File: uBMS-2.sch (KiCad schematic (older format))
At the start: 65 parts

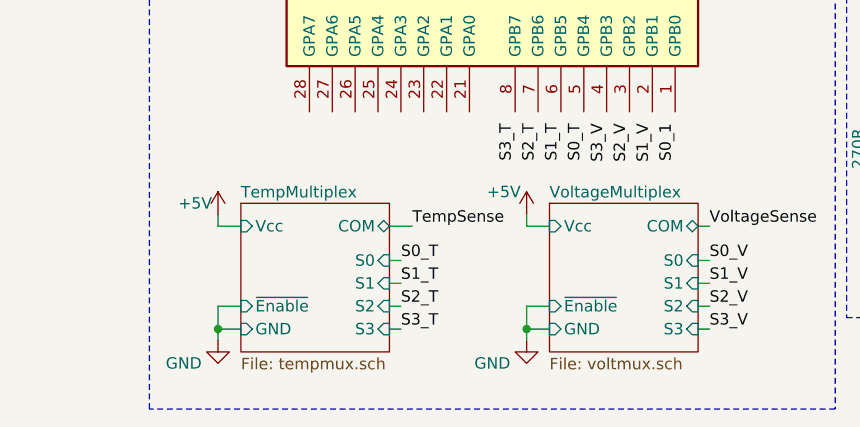
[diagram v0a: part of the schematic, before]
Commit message: Work on Voltage Sheet
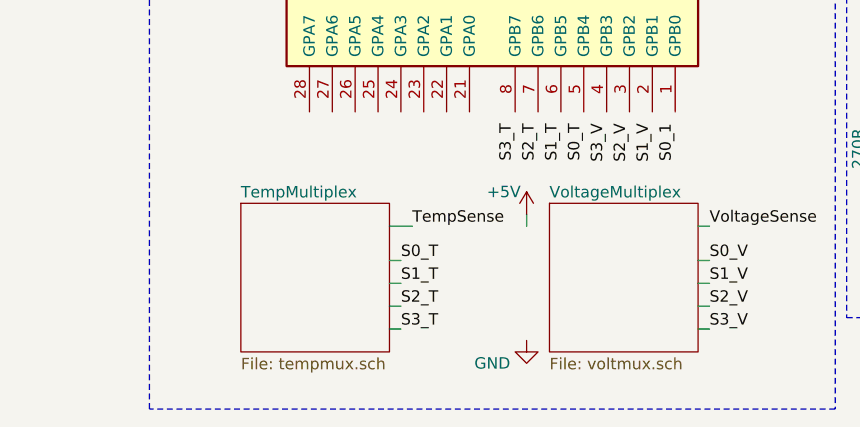
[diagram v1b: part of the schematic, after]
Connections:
- wire segments 241 -> 230
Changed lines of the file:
@@
 F0 "VoltageMultiplex" 50
 F1 "voltmux.sch" 50
-F2 "S0" I R 7150 5800 50
-F3 "S1" I R 7150 5900 50
-F4 "S2" I R 7150 6000 50
-F5 "S3" I R 7150 6100 50
-F6 "COM" B R 7150 5650 50
-F7 "GND" I L 6500 6100 50
-F8 "~Enable~" I L 6500 6000 50
-F9 "Vcc" I L 6500 5650 50
 $EndSheet
 $Sheet
@@
 F0 "TempMultiplex" 50
 F1 "tempmux.sch" 50
-F2 "S3" I R 5800 6100 50
-F3 "S2" I R 5800 6000 50
-F4 "S1" I R 5800 5900 50
-F5 "S0" I R 5800 5800 50
-F6 "COM" B R 5800 5650 50
-F7 "GND" I L 5150 6100 50
-F8 "~Enable~" I L 5150 6000 50
-F9 "Vcc" I L 5150 5650 50
 $EndSheet
 $Comp
@@
 $EndComp
 Wire Wire Line
-	6400 6150 6400 6100
-Wire Wire Line
-	6400 6100 6500 6100
-Wire Wire Line
 	6400 5650 6400 5600
-Wire Wire Line
-	6400 5650 6500 5650
-Wire Wire Line
-	6400 6000 6400 6100
-Connection ~ 6400 6100
-Wire Wire Line
-	6400 6000 6500 6000
-$Comp
-L power:GND #PWR?
-U 1 1 5F399A72
-P 5050 6150
-F 0 "#PWR?" H 5050 5900 50  0001 C CNN
-F 1 "GND" H 4900 6050 50  0000 C CNN
-F 2 "" H 5050 6150 50  0001 C CNN
-F 3 "" H 5050 6150 50  0001 C CNN
-	1    5050 6150
-	1    0    0    -1
-$EndComp
-Wire Wire Line
-	5050 6150 5050 6100
-Wire Wire Line
-	5050 6100 5150 6100
-Wire Wire Line
-	5050 6100 5050 6000
-Wire Wire Line
-	5050 6000 5150 6000
-Connection ~ 5050 6100
-$Comp
-L power:+5V #PWR?
-U 1 1 5F3B6840
-P 5050 5600
-F 0 "#PWR?" H 5050 5450 50  0001 C CNN
-F 1 "+5V" H 4950 5650 50  0000 C CNN
-F 2 "" H 5050 5600 50  0001 C CNN
-F 3 "" H 5050 5600 50  0001 C CNN
-	1    5050 5600
-	1    0    0    -1
-$EndComp
-Wire Wire Line
-	5050 5600 5050 5650
-Wire Wire Line
-	5050 5650 5150 5650
 Text Label 7200 5650 0    50   ~ 0
 VoltageSense

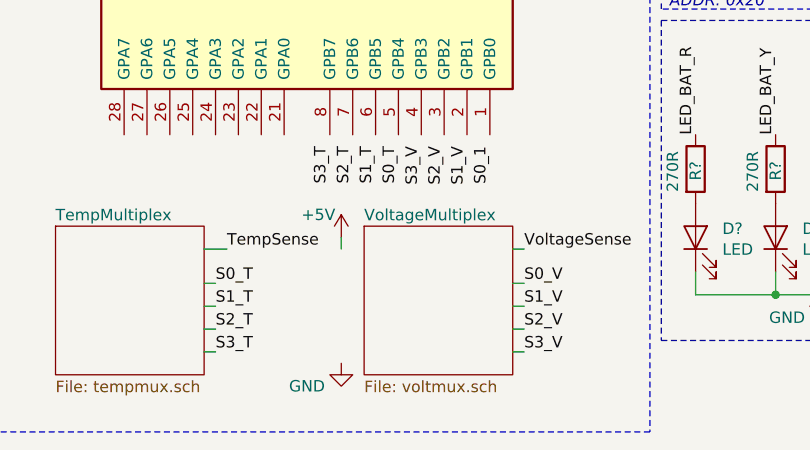
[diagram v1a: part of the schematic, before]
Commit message: Finished voltage sense sheet
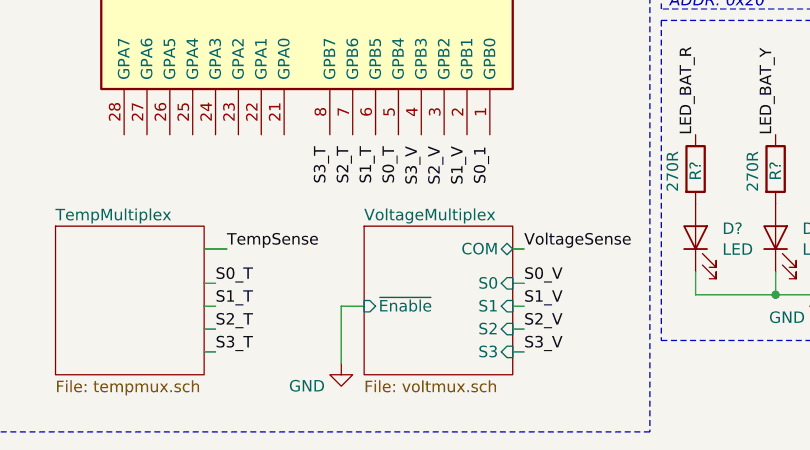
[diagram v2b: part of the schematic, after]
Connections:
- wire segments 230 -> 231
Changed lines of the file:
@@
 F0 "VoltageMultiplex" 50
 F1 "voltmux.sch" 50
+F2 "S0" I R 7150 5800 50
+F3 "S1" I R 7150 5900 50
+F4 "S2" I R 7150 6000 50
+F5 "S3" I R 7150 6100 50
+F6 "COM" B R 7150 5650 50
+F7 "~Enable~" I L 6500 5900 50
 $EndSheet
 $Sheet
@@
 	7550 2900 7550 2800
 $Comp
-L power:+5V #PWR?
-U 1 1 5F353B75
-P 6400 5600
-F 0 "#PWR?" H 6400 5450 50  0001 C CNN
-F 1 "+5V" H 6300 5700 50  0000 C CNN
-F 2 "" H 6400 5600 50  0001 C CNN
-F 3 "" H 6400 5600 50  0001 C CNN
-	1    6400 5600
-	1    0    0    -1
-$EndComp
-$Comp
 L power:GND #PWR?
 U 1 1 5F3615AC
@@
 	1    0    0    -1
 $EndComp
-Wire Wire Line
-	6400 5650 6400 5600
 Text Label 7200 5650 0    50   ~ 0
 VoltageSense
@@
 Wire Notes Line
 	4750 6450 4750 3500
+Wire Wire Line
+	6500 5900 6400 5900
+Wire Wire Line
+	6400 5900 6400 6150
 $EndSCHEMATC

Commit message: Finished Temp Sheet
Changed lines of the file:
@@
 F0 "TempMultiplex" 50
 F1 "tempmux.sch" 50
+F2 "S0" I R 5800 5800 50
+F3 "S1" I R 5800 5900 50
+F4 "S2" I R 5800 6000 50
+F5 "S3" I R 5800 6100 50
+F6 "COM" B R 5800 5650 50
+F7 "~Enable~" I L 5150 5900 50
 $EndSheet
 $Comp
@@
 Wire Wire Line
 	6400 5900 6400 6150
+$Comp
+L power:GND #PWR?
+U 1 1 5F6C7C43
+P 5050 6150
+F 0 "#PWR?" H 5050 5900 50  0001 C CNN
+F 1 "GND" H 4900 6050 50  0000 C CNN
+F 2 "" H 5050 6150 50  0001 C CNN
+F 3 "" H 5050 6150 50  0001 C CNN
+	1    5050 6150
+	1    0    0    -1
+$EndComp
+Wire Wire Line
+	5150 5900 5050 5900
+Wire Wire Line
+	5050 5900 5050 6150
 $EndSCHEMATC

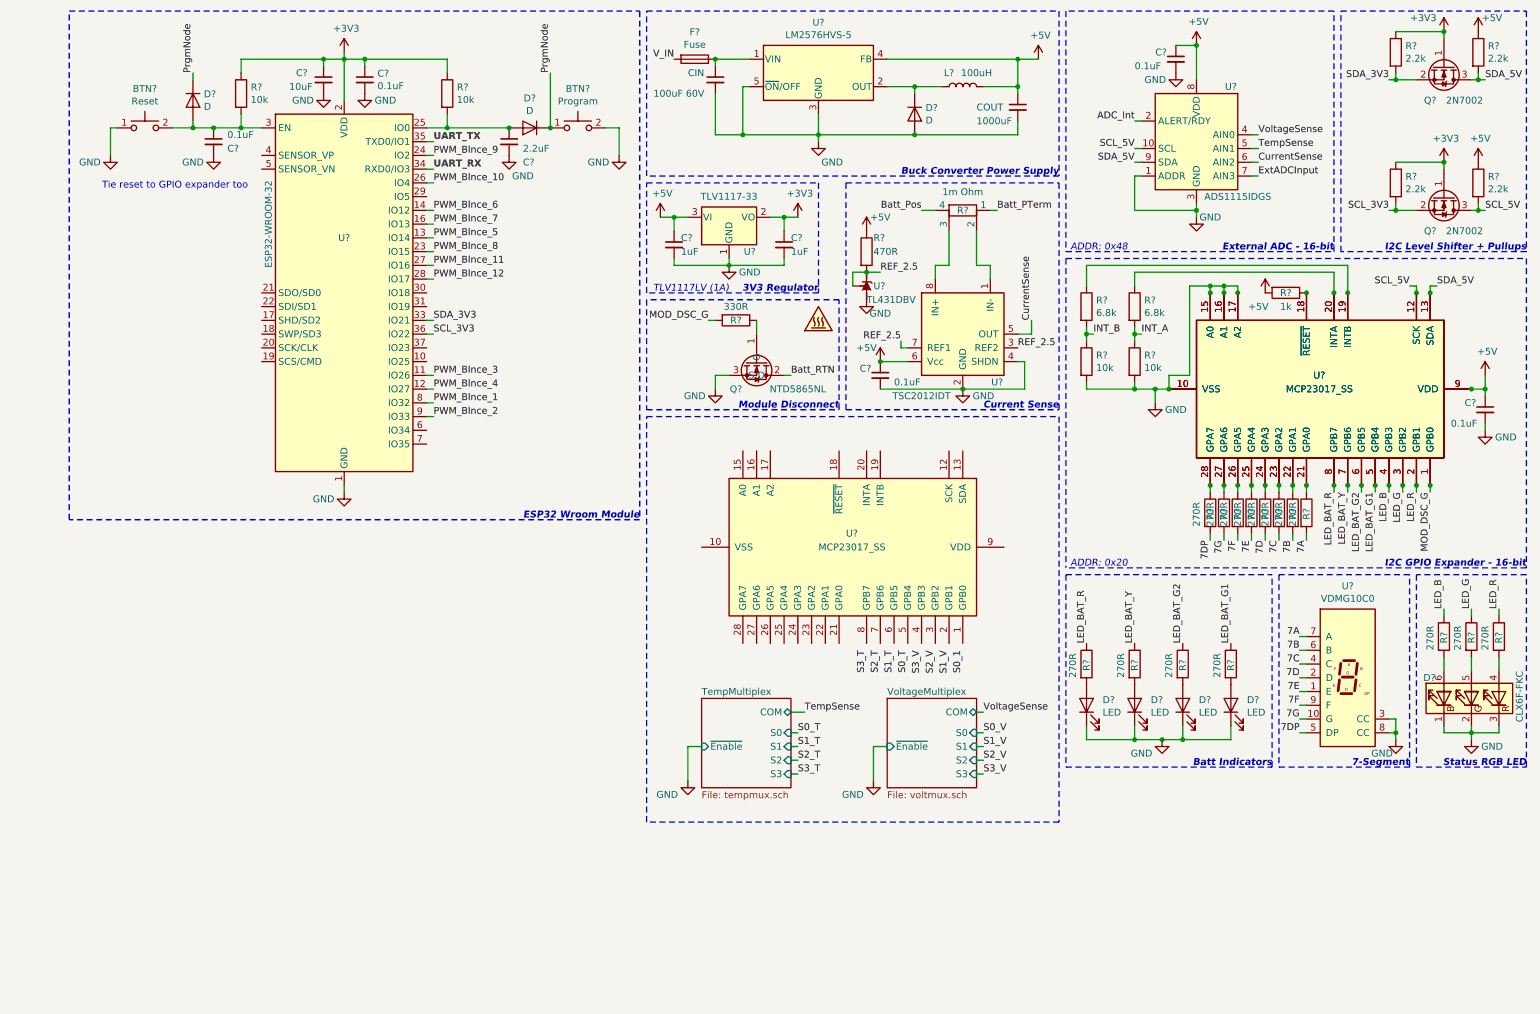
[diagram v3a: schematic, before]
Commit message: Wired up second GPIO expander and reset pins
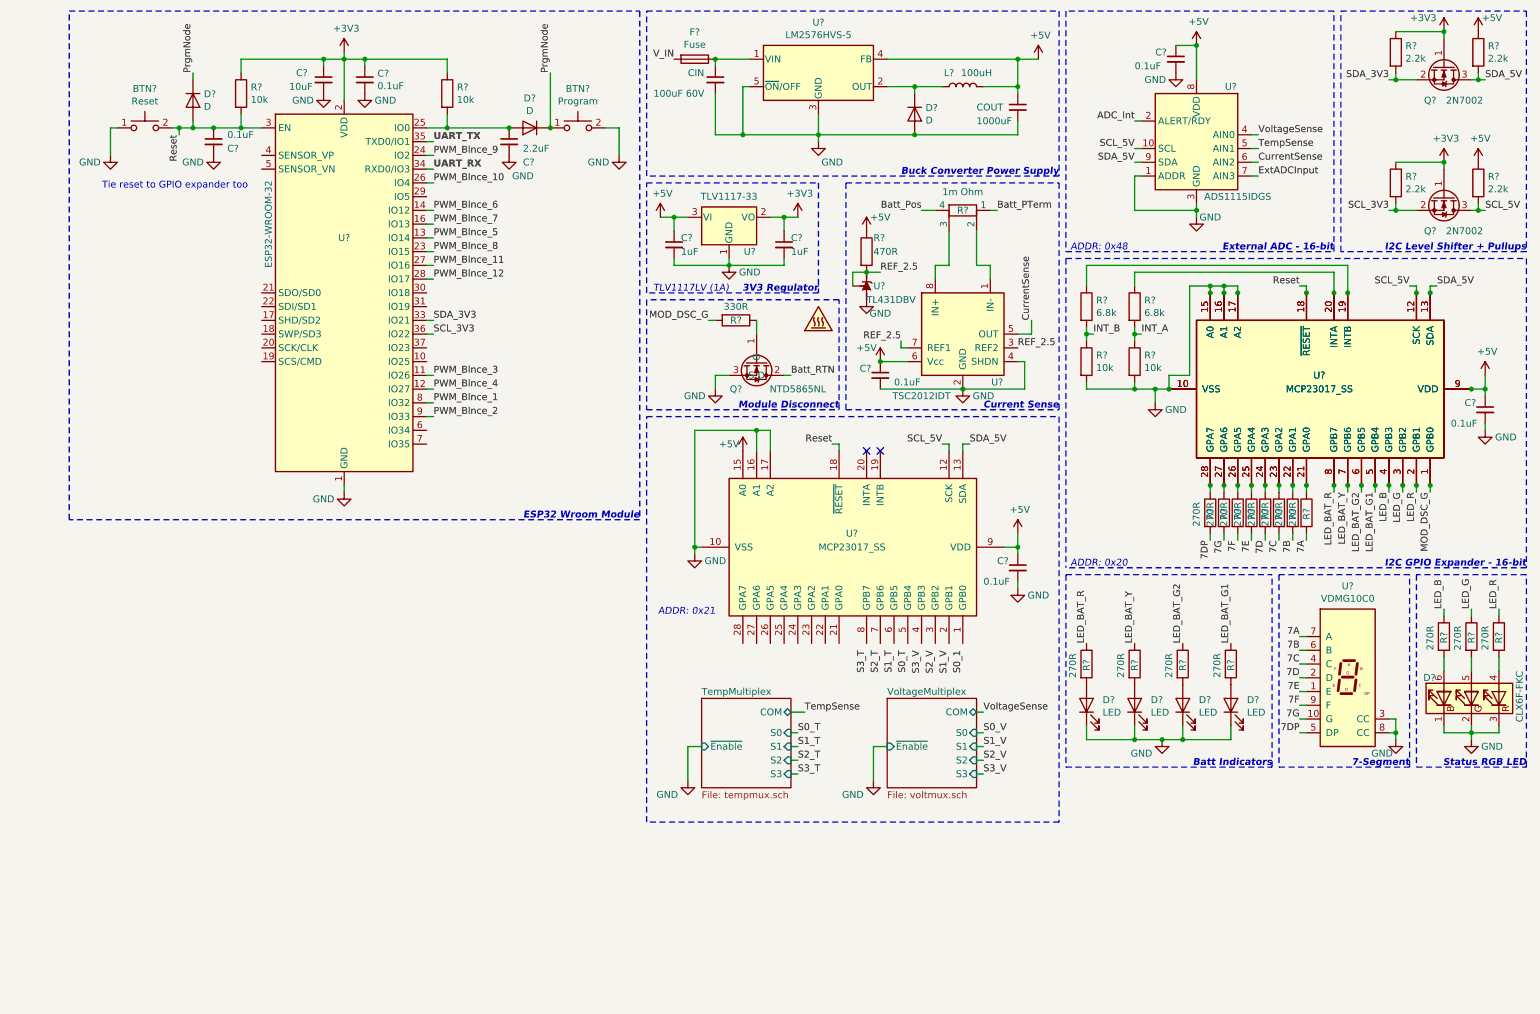
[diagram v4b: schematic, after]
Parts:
- removed R?: 1k, symbol Device:R
- added C?: 0.1uF, symbol Device:C_Small
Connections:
- net +5V: now also U?.15 (A0), U?.9 (VDD), C?.1
- net GND: now also U?.10 (VSS), U?.16 (A1), U?.17 (A2), C?.2
- net SCL_5V: now also U?.12 (SCK)
- net SDA_5V: now also U?.13 (SDA)
- net Reset: now reaches BTN?.2, C?.1, D?.2 (A), R?.2, U?.3 (EN)
- net Reset: now also U?.18 (~RESET~), U?.18 (~RESET~), U?.18 (~RESET~)
- no-connect marks 0 -> 2
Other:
- note added: "ADDR: 0x21"
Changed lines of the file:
@@
 	850  1400 900  1400
 Wire Wire Line
-	1300 1400 1450 1400
+	1300 1400 1350 1400
 $Comp
 L Device:R R?
@@
 	8550 3200 8550 3300
 Connection ~ 8850 2550
-$Comp
-L Device:R R?
-U 1 1 5F3AC1C4
-P 9400 2600
-F 0 "R?" V 9400 2600 50  0000 C CNN
-F 1 "1k" V 9500 2600 50  0000 C CNN
-F 2 "" V 9330 2600 50  0001 C CNN
-F 3 "~" H 9400 2600 50  0001 C CNN
-	1    9400 2600
-	0    1    1    0
-$EndComp
-$Comp
-L power:+5V #PWR?
-U 1 1 5F3B2689
-P 9250 2600
-F 0 "#PWR?" H 9250 2450 50  0001 C CNN
-F 1 "+5V" H 9200 2500 50  0000 C CNN
-F 2 "" H 9250 2600 50  0001 C CNN
-F 3 "" H 9250 2600 50  0001 C CNN
-	1    9250 2600
-	1    0    0    -1
-$EndComp
 Wire Wire Line
 	9750 2600 9750 2450
@@
 	8300 2450 8300 2550
 Connection ~ 9750 2600
-Connection ~ 9550 2600
 Wire Wire Line
 	9850 2600 9850 2400
@@
 Wire Wire Line
 	5050 5900 5050 6150
+$Comp
+L power:+5V #PWR?
+U 1 1 5F6D905B
+P 5450 3750
+F 0 "#PWR?" H 5450 3600 50  0001 C CNN
+F 1 "+5V" H 5350 3800 50  0000 C CNN
+F 2 "" H 5450 3750 50  0001 C CNN
+F 3 "" H 5450 3750 50  0001 C CNN
+	1    5450 3750
+	1    0    0    -1
+$EndComp
+$Comp
+L power:GND #PWR?
+U 1 1 5F6D9988
+P 5100 4500
+F 0 "#PWR?" H 5100 4250 50  0001 C CNN
+F 1 "GND" H 5250 4450 50  0000 C CNN
+F 2 "" H 5100 4500 50  0001 C CNN
+F 3 "" H 5100 4500 50  0001 C CNN
+	1    5100 4500
+	1    0    0    -1
+$EndComp
+Wire Wire Line
+	5100 4500 5100 4450
+Wire Wire Line
+	5100 4450 5150 4450
+Wire Wire Line
+	5550 3750 5550 3600
+Wire Wire Line
+	5550 3600 5100 3600
+Wire Wire Line
+	5100 3600 5100 4450
+Connection ~ 5100 4450
+Wire Wire Line
+	5650 3750 5650 3600
+Wire Wire Line
+	5650 3600 5550 3600
+Connection ~ 5550 3600
+NoConn ~ 6350 3750
+NoConn ~ 6450 3750
+Text Label 1350 1450 3    50   ~ 0
+Reset
+Wire Wire Line
+	1350 1450 1350 1400
+Connection ~ 1350 1400
+Wire Wire Line
+	1350 1400 1450 1400
+Text Label 9500 2550 2    50   ~ 0
+Reset
+Text Label 6100 3700 2    50   ~ 0
+Reset
+Wire Wire Line
+	6150 3750 6150 3700
+Wire Wire Line
+	6150 3700 6100 3700
+Wire Wire Line
+	9550 2600 9550 2550
+Wire Wire Line
+	9550 2550 9500 2550
+Connection ~ 9550 2600
+Text Notes 5250 4950 2    50   Italic 0
+ADDR: 0x21
+$Comp
+L power:GND #PWR?
+U 1 1 5F75DAB6
+P 7450 4750
+F 0 "#PWR?" H 7450 4500 50  0001 C CNN
+F 1 "GND" H 7600 4700 50  0000 C CNN
+F 2 "" H 7450 4750 50  0001 C CNN
+F 3 "" H 7450 4750 50  0001 C CNN
+	1    7450 4750
+	1    0    0    -1
+$EndComp
+$Comp
+L power:+5V #PWR?
+U 1 1 5F75DABC
+P 7450 4350
+F 0 "#PWR?" H 7450 4200 50  0001 C CNN
+F 1 "+5V" H 7465 4523 50  0000 C CNN
+F 2 "" H 7450 4350 50  0001 C CNN
+F 3 "" H 7450 4350 50  0001 C CNN
+	1    7450 4350
+	1    0    0    -1
+$EndComp
+$Comp
+L Device:C_Small C?
+U 1 1 5F75DAC2
+P 7450 4600
+F 0 "C?" H 7300 4650 50  0000 L CNN
+F 1 "0.1uF" H 7200 4500 50  0000 L CNN
+F 2 "" H 7450 4600 50  0001 C CNN
+F 3 "~" H 7450 4600 50  0001 C CNN
+	1    7450 4600
+	1    0    0    -1
+$EndComp
+Wire Wire Line
+	7350 4450 7450 4450
+Wire Wire Line
+	7450 4450 7450 4350
+Connection ~ 7450 4450
+Wire Wire Line
+	7450 4500 7450 4450
+Wire Wire Line
+	7450 4700 7450 4750
+Text Label 7100 3700 0    50   ~ 0
+SDA_5V
+Text Label 6900 3700 2    50   ~ 0
+SCL_5V
+Wire Wire Line
+	6950 3750 6950 3700
+Wire Wire Line
+	6950 3700 6900 3700
+Wire Wire Line
+	7050 3750 7050 3700
+Wire Wire Line
+	7050 3700 7100 3700
 $EndSCHEMATC

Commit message: Finished Balance Sheet
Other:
- note added: "I2C GPIO Expander & Voltage & Temp Sense"
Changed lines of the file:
@@
 $Descr A4 11693 8268
 encoding utf-8
-Sheet 1 3
+Sheet 1 4
 Title "Micro BMS v2"
 Date ""
@@
 Wire Wire Line
 	7050 3700 7100 3700
+Text Notes 7450 6450 2    50   Italic 10
+I2C GPIO Expander & Voltage & Temp Sense
+$Sheet
+S 3000 4500 1500 1000
+U 5F7870B7
+F0 "BatteryBalance" 50
+F1 "BatteryBalance.sch" 50
+$EndSheet
 $EndSCHEMATC
